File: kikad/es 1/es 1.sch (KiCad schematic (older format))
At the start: 4 parts

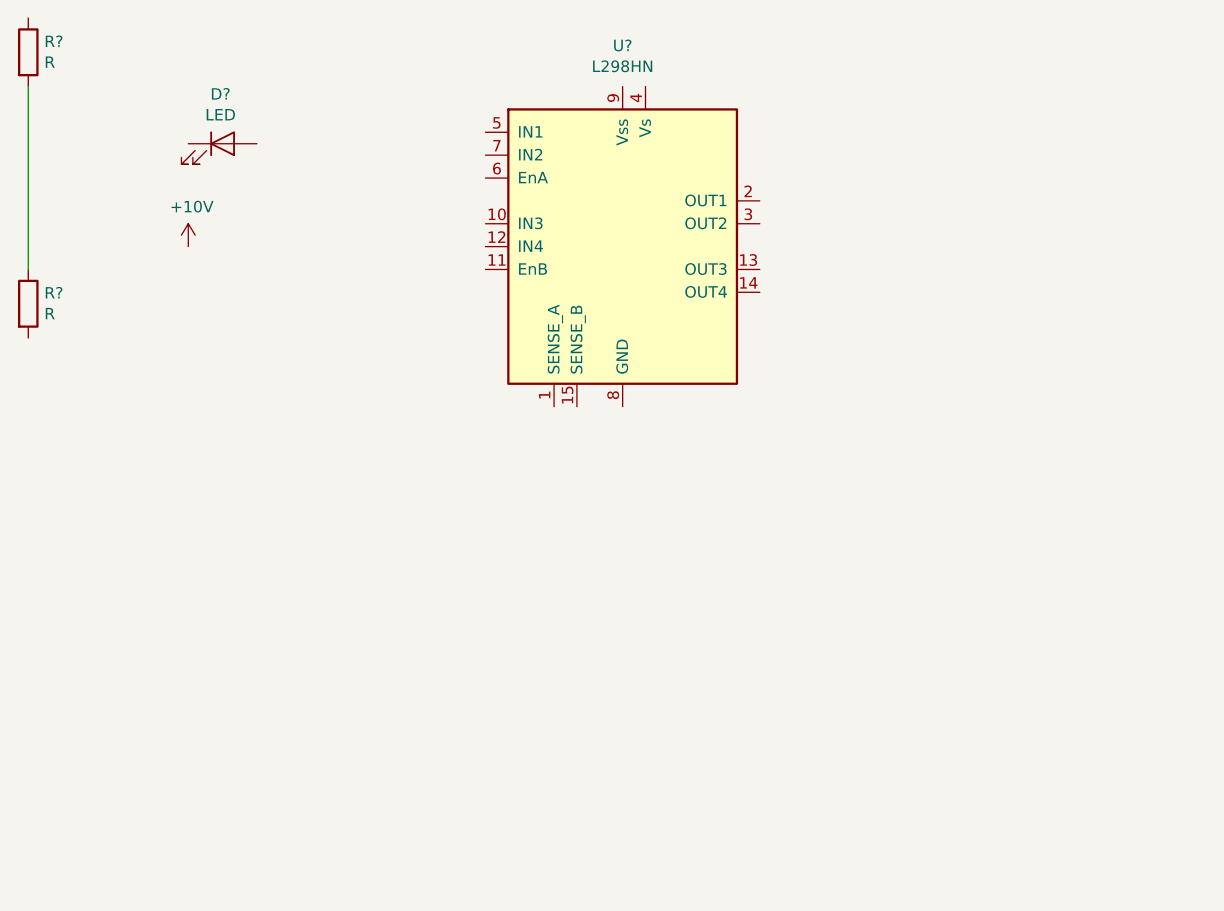
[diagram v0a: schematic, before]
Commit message: es 1 (led, potenziometro, pulsante)
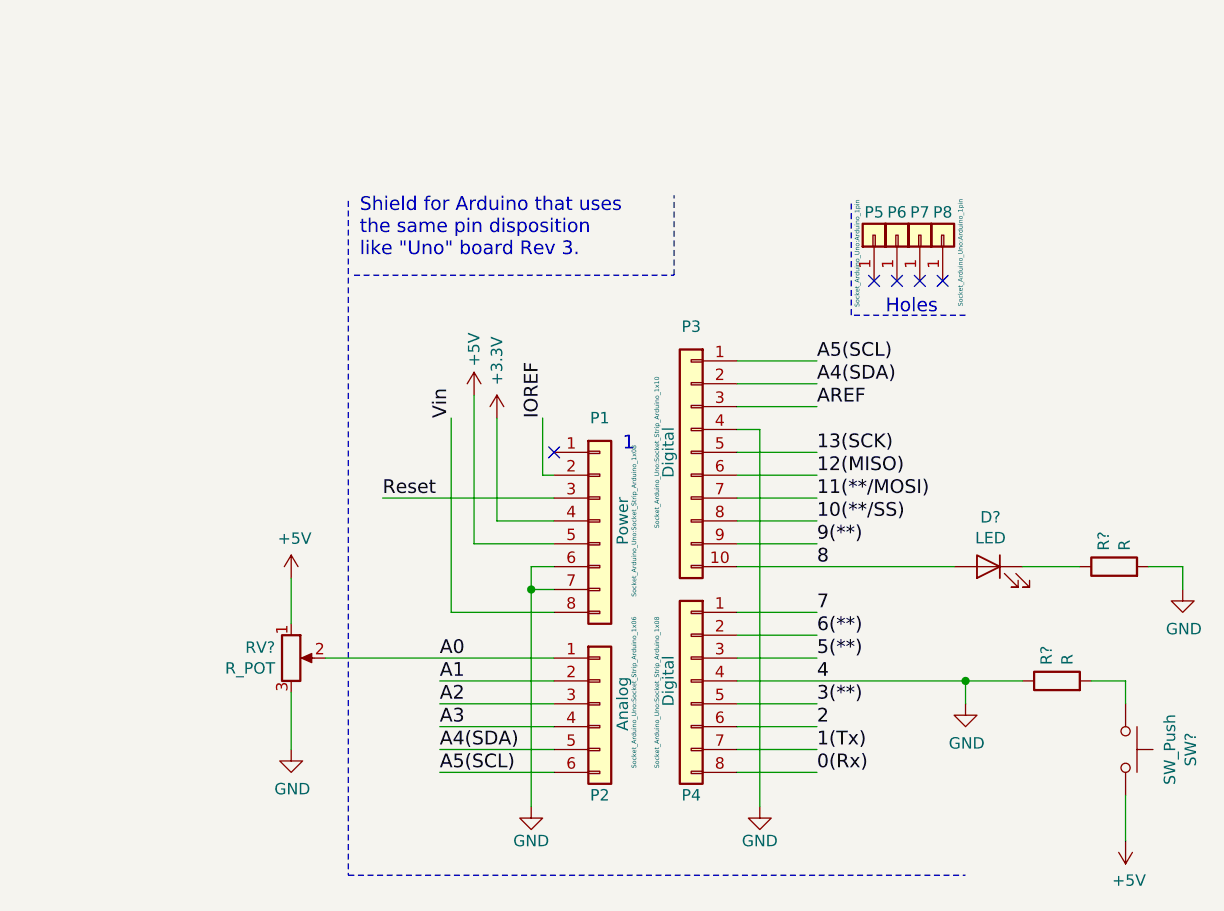
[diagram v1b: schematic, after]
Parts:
- removed D?: LED, symbol Device:LED
- removed R? (x2): R, symbol Device:R
- removed U?: L298HN, Package_TO_SOT_THT:TO-220-15_P2.54x2.54mm_StaggerOdd_Lead4.58mm_Vertical, symbol Driver_Motor:L298HN
- added D?: LED, symbol Device:LED
- added P1: Power, Socket_Arduino_Uno:Socket_Strip_Arduino_1x08, symbol Connector_Generic:Conn_01x08
- added P2: Analog, Socket_Arduino_Uno:Socket_Strip_Arduino_1x06, symbol Connector_Generic:Conn_01x06
- added P3: Digital, Socket_Arduino_Uno:Socket_Strip_Arduino_1x10, symbol Connector_Generic:Conn_01x10
- added P4: Digital, Socket_Arduino_Uno:Socket_Strip_Arduino_1x08, symbol Connector_Generic:Conn_01x08
- added P5, P6, P7, P8: CONN_01X01, Socket_Arduino_Uno:Arduino_1pin, symbol Connector_Generic:Conn_01x01
- added R? (x2): R, symbol Device:R
- added RV?: R_POT, symbol Device:R_POT
- added SW?: SW_Push, symbol Switch:SW_Push
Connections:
- new net: D?.1 (K), R?.1
- new net: R?.2, SW?.2
- new net +3V3: P1.4 (Pin_4)
- new net +5V: P1.5 (Pin_5), RV?.1, SW?.1
- new net 0(Rx): P4.8 (Pin_8)
- new net 1(Tx): P4.7 (Pin_7)
- new net 10(**/SS): P3.8 (Pin_8)
- new net 11(**/MOSI): P3.7 (Pin_7)
- new net 12(MISO): P3.6 (Pin_6)
- new net 13(SCK): P3.5 (Pin_5)
- new net 2: P4.6 (Pin_6)
- new net 3(**): P4.5 (Pin_5)
- new net 5(**): P4.3 (Pin_3)
- new net 6(**): P4.2 (Pin_2)
- new net 7: P4.1 (Pin_1)
- new net 8: D?.2 (A), P3.10 (Pin_10)
- new net 9(**): P3.9 (Pin_9)
- new net A0: P2.1 (Pin_1), RV?.2
- new net A1: P2.2 (Pin_2)
- new net A2: P2.3 (Pin_3)
- new net A3: P2.4 (Pin_4)
- new net A4(SDA): P2.5 (Pin_5), P3.2 (Pin_2)
- new net A5(SCL): P2.6 (Pin_6), P3.1 (Pin_1)
- new net AREF: P3.3 (Pin_3)
- new net GND: P1.6 (Pin_6), P1.7 (Pin_7), P3.4 (Pin_4), P4.4 (Pin_4), R?.1, R?.2, RV?.3
- new net IOREF: P1.2 (Pin_2)
- new net Reset: P1.3 (Pin_3)
- new net Vin: P1.8 (Pin_8)
- no-connect marks 0 -> 5
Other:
- note added: "1"
- note added: "Holes"
- note added: "Shield for Arduino that uses\nthe same pin disposition\nlike "Uno" board Rev 3."
